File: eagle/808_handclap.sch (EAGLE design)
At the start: 94 parts, among them IC1 LM339N, IC2 TL072P, IC3 TL072P, Q28 BC546, Q29 BC556, Q35 BC546, Q69 BC546, Q70 BC546, Q71 BC556, Q72 BC556, Q73 BC546, U1 POWER, U22 BA6110SIL

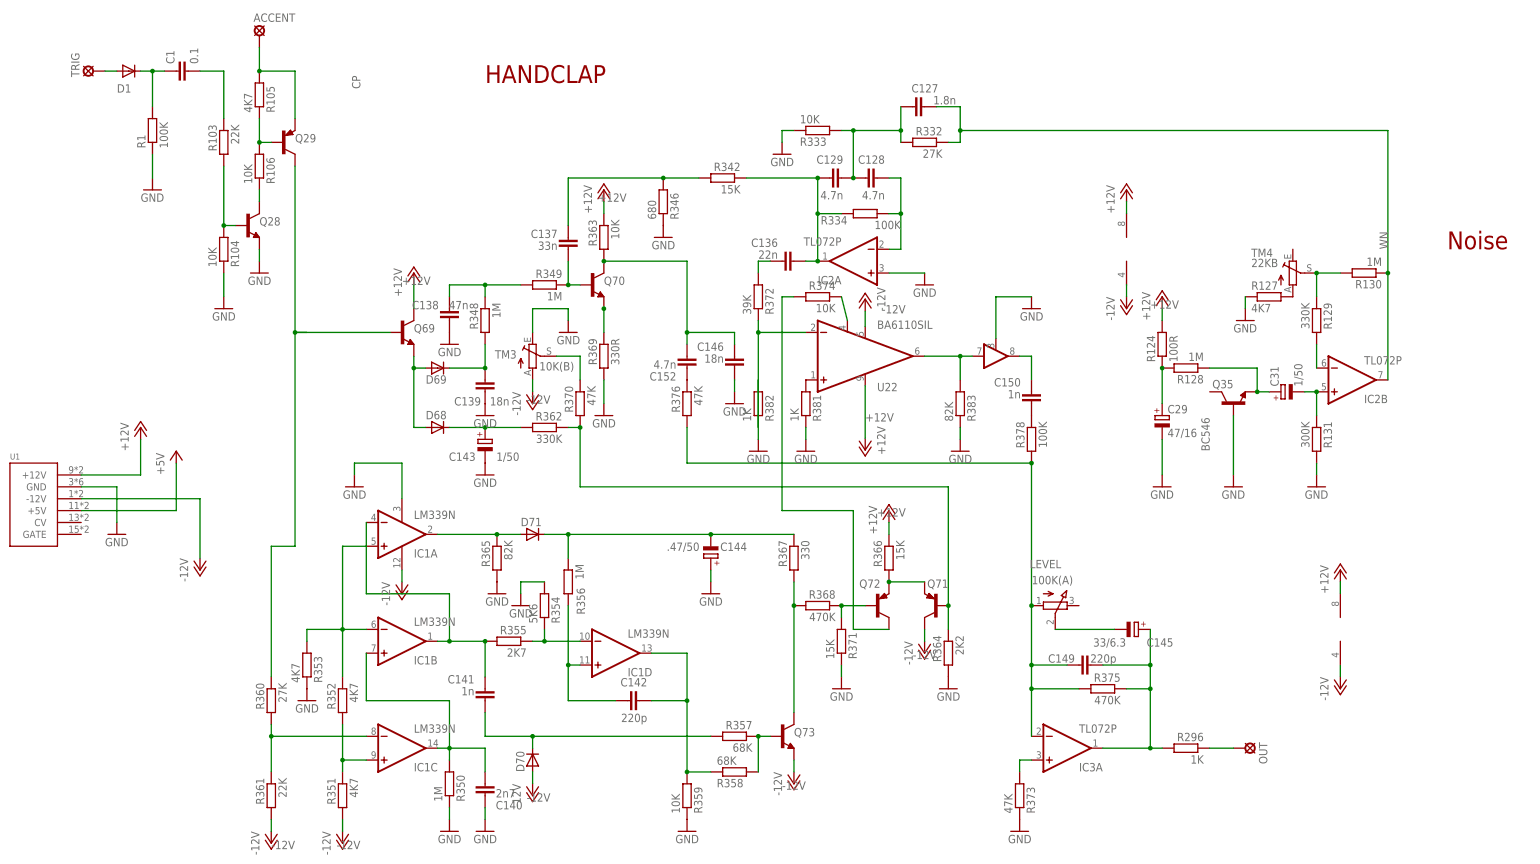
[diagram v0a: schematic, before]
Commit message: 2n3904 and 2n3906
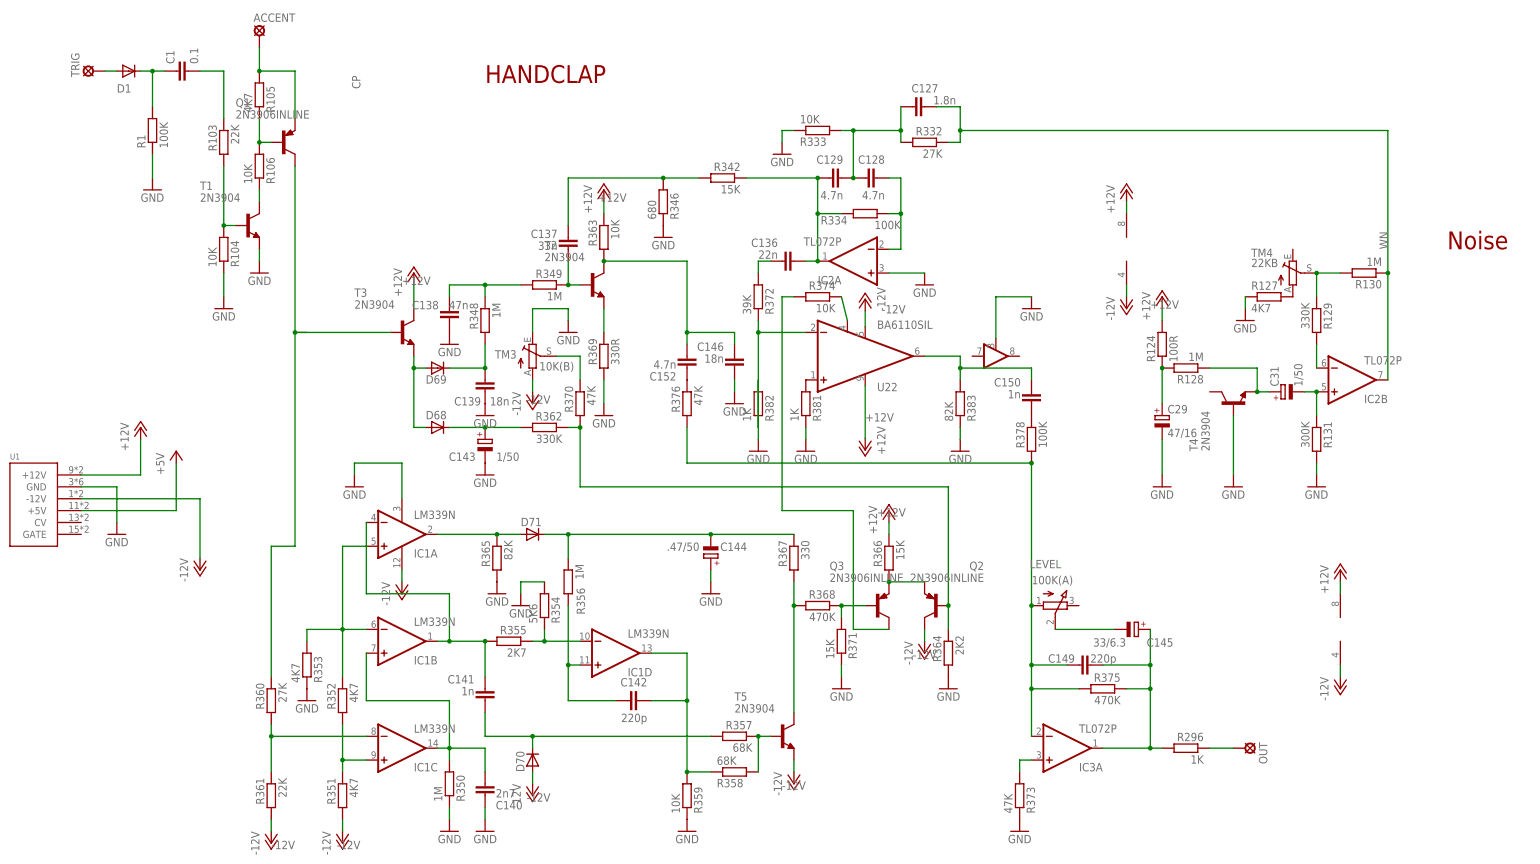
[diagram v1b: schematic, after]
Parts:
- removed Q28, Q35, Q69, Q70, Q73: BC546, transistor:BC546-NPN-TO92-CBE
- removed Q29: BC556, transistor:BC556B-PNP-TO92-EBC
- removed Q71, Q72: BC556, transistor:BC556A-PNP-TO92-EBC
- added Q1, Q2, Q3: 2N3906INLINE, mes_transistors:2N3906INLINE
- added T1, T2, T3, T4, T5: 2N3904, transistor:2N3904
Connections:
- removed net N$63: C150.1, U22.OUT1
- net +12V: now also T3.C; no longer Q69.C
- net -12V: now also Q2.C, T5.E; no longer Q71.C, Q73.E
- net CPTRIG: now also Q1.C, T3.B; no longer Q29.C, Q69.B
- net GND: now also T1.E, T4.B; no longer Q28.E, Q35.B
- net N$37: now also Q1.B; no longer Q29.B
- net N$38: now also T1.C; no longer Q28.C
- net N$4: now also T1.B; no longer Q28.B
- net N$40: now also T2.B; no longer Q70.B
- net N$42: now also T2.E; no longer Q70.E
- net N$44: now also T3.E; no longer Q69.E
- net N$46: now also T2.C; no longer Q70.C
- net N$48: now also Q2.B; no longer Q71.B
- net N$61: now also C150.1; no longer U22.IN1
- net N$66: now also Q3.B; no longer Q72.B
- net N$67: now also Q2.E, Q3.E; no longer Q71.E, Q72.E
- net N$69: now also Q3.C; no longer Q72.C
- net N$695: now also T4.E; no longer Q35.E
- net N$70: now also T5.C; no longer Q73.C
- net N$75: now also T5.B; no longer Q73.B
- net TRIG: now also Q1.E; no longer Q29.E

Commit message: gcode for converted version
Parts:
- R124, R296: device TR808clone:R-EU_0207/5V -> TR808clone:R-EU_0207/7
- R375: device TR808clone:R-EU_0207/2V -> TR808clone:R-EU_0207/7
- T1, T2, T3, T4, T5: value 2N3904 -> 2N3904INLINE; device transistor:2N3904 -> bt_transistor:2N3904INLINE
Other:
- moved on the sheet: C127, R130, R296, R382, TM4
